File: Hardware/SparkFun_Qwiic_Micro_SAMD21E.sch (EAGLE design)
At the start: 41 parts, among them Q1 3.1A/30V/105mΩ, U1 3.3V, U2 W25Q32FV, U3 SAMD21E

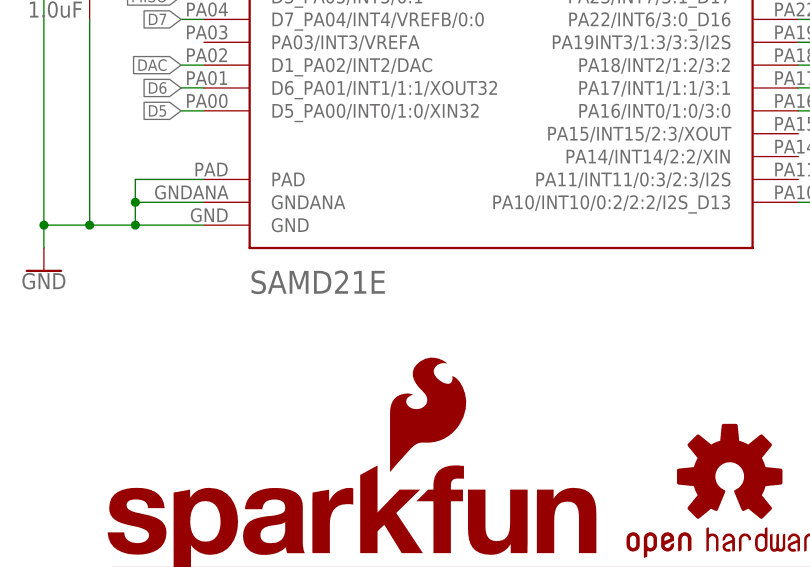
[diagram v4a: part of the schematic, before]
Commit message: New bootloader, updates samd21 with latest package
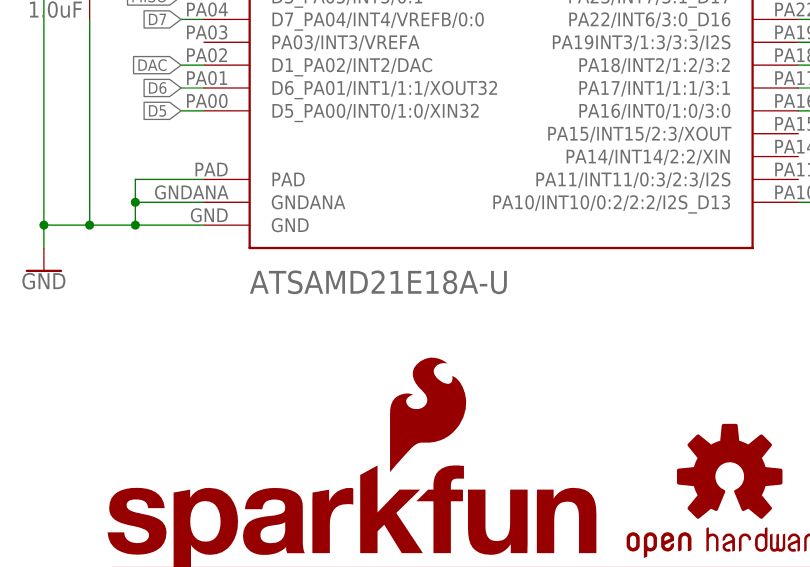
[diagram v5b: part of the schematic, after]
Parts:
- U3: value SAMD21E -> ATSAMD21E18A-U; device SparkFun-IC-Microcontroller:SAMD21E -> SparkFun-IC-Microcontroller:ATSAMD21E18A-U
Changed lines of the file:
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@@
 <part name="GND3" library="SparkFun-PowerSymbols" deviceset="GND" device=""/>
 <part name="SUPPLY14" library="SparkFun-PowerSymbols" deviceset="V_USB" device=""/>
-<part name="U3" library="SparkFun-IC-Microcontroller" deviceset="SAMD21E" device=""/>
+<part name="U3" library="SparkFun-IC-Microcontroller" deviceset="ATSAMD21E18A-U" device=""/>
 <part name="SUPPLY11" library="SparkFun-PowerSymbols" deviceset="V_USB" device=""/>
 <part name="JP1" library="SparkFun-Jumpers" deviceset="JUMPER-SMT_2_NC_TRACE" device="_SILK" value="LED"/>

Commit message: Moves 10k pull-up resistor on Flash CS line to top layer.
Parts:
- R2: device SparkFun-Resistors:10KOHM-0603-1/10W-1% -> SparkFun-Resistors:10KOHM-0402-1/16W-1%
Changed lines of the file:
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@@
 <?xml version="1.0" encoding="utf-8"?>
 <!DOCTYPE eagle SYSTEM "eagle.dtd">
-<eagle version="9.4.0">
+<eagle version="9.4.2">
 <drawing>
 <settings>
@@
 <part name="GND8" library="SparkFun-PowerSymbols" deviceset="GND" device=""/>
 <part name="GND4" library="SparkFun-PowerSymbols" deviceset="GND" device=""/>
-<part name="R2" library="SparkFun-Resistors" deviceset="10KOHM" device="-0603-1/10W-1%" value="10k"/>
+<part name="R2" library="SparkFun-Resistors" deviceset="10KOHM" device="-0402-1/16W-1%" value="10k"/>
 <part name="SUPPLY8" library="SparkFun-PowerSymbols" deviceset="3.3V" device=""/>
 <part name="D1" library="SparkFun-DiscreteSemi" deviceset="DIODE-SCHOTTKY" device="-BAT20J" value="1A/23V/620mV"/>

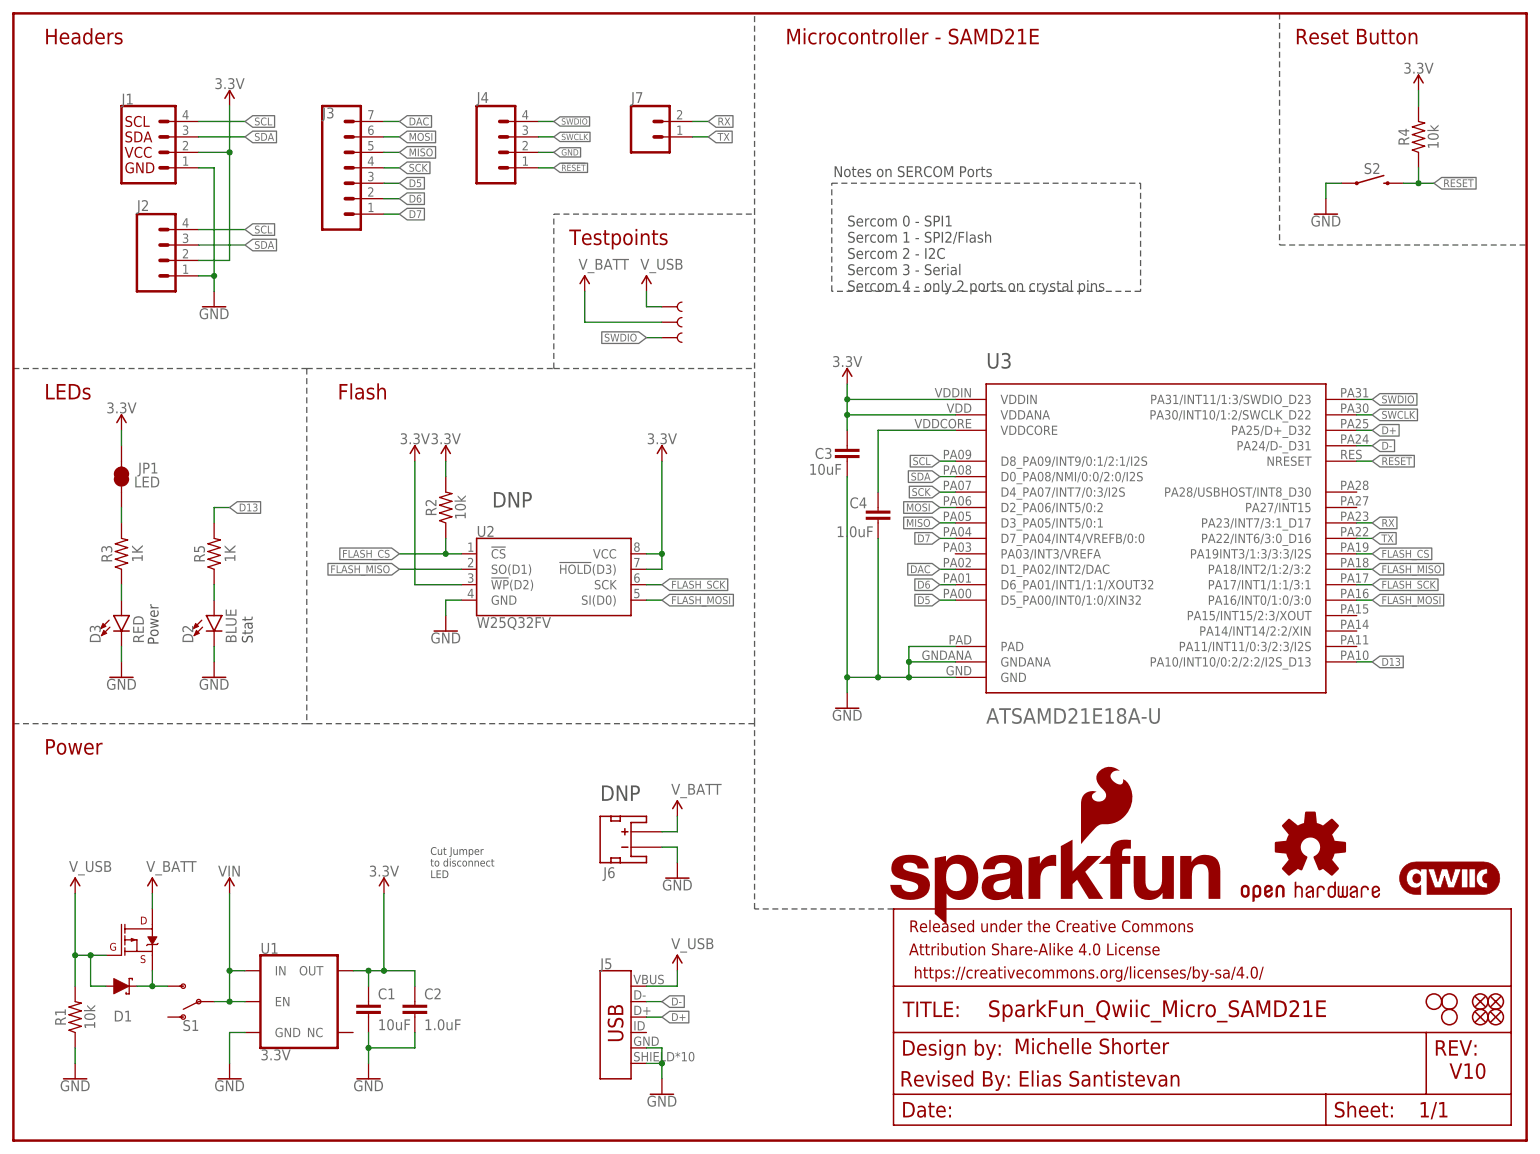
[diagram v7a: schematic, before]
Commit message: Adds VCC ranges, Adds note for optional parts
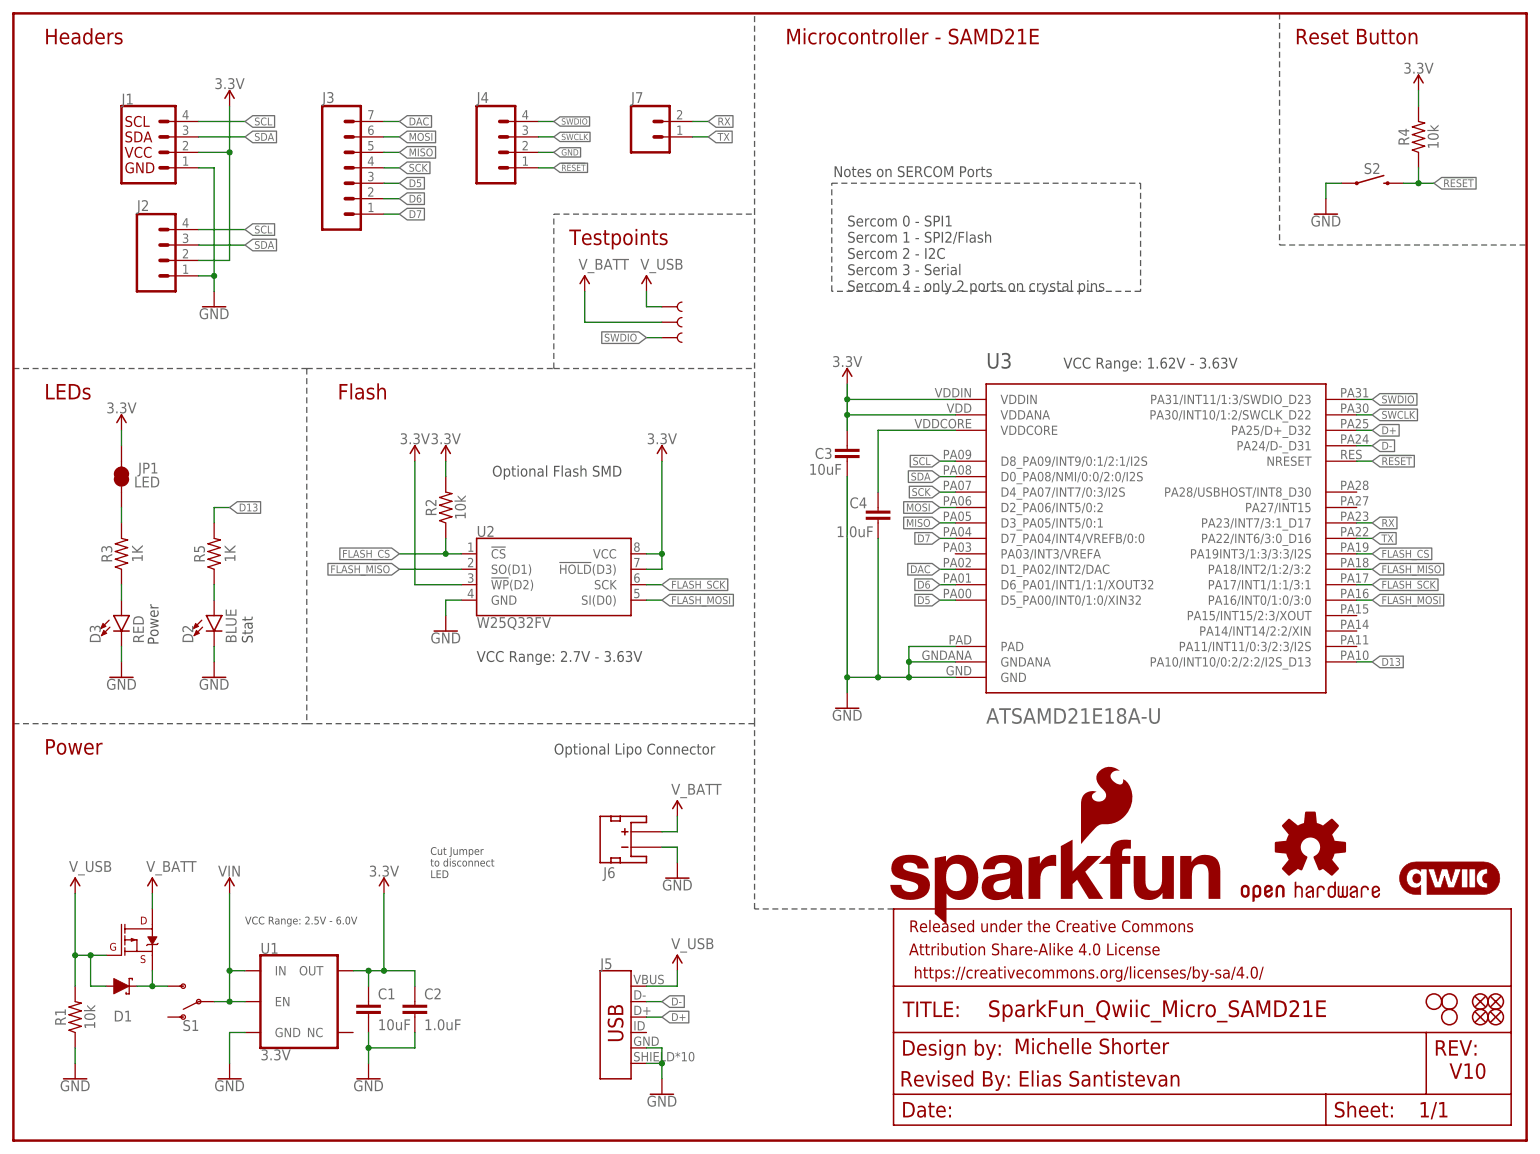
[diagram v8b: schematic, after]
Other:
- note added: "Optional Flash SMD"
- note added: "Optional Lipo Connector"
- note added: "VCC Range: 1.62V - 3.63V"
- note added: "VCC Range: 2.5V - 6.0V"
- note added: "VCC Range: 2.7V - 3.63V"
- note removed: "DNP"
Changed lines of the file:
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@@
 <?xml version="1.0" encoding="utf-8"?>
 <!DOCTYPE eagle SYSTEM "eagle.dtd">
-<eagle version="9.4.0">
+<eagle version="9.4.2">
 <drawing>
 <settings>
@@
 <text x="5.08" y="63.5" size="2.54" layer="94" font="vector">Power</text>
 <text x="127" y="180.34" size="2.54" layer="94" font="vector">Microcontroller - SAMD21E</text>
-<text x="78.74" y="104.14" size="2.54" layer="97" font="vector">DNP</text>
-<text x="96.52" y="55.88" size="2.54" layer="97" font="vector">DNP</text>
+<text x="78.74" y="109.22" size="1.778" layer="97" font="vector">Optional Flash SMD</text>
 <text x="236.22" y="10.16" size="2.54" layer="94" font="vector">V10</text>
 <text x="164.592" y="14.224" size="2.54" layer="94" font="vector">Michelle Shorter</text>
@@
 <text x="39.37" y="81.788" size="1.778" layer="97" font="vector" rot="R90">Stat</text>
 <text x="23.876" y="81.534" size="1.778" layer="97" font="vector" rot="R90">Power</text>
+<text x="38.1" y="35.56" size="1.27" layer="97" font="vector">VCC Range: 2.5V - 6.0V</text>
+<text x="172.72" y="127" size="1.778" layer="97" font="vector">VCC Range: 1.62V - 3.63V</text>
+<text x="76.2" y="78.74" size="1.778" layer="97" font="vector">VCC Range: 2.7V - 3.63V</text>
+<text x="88.9" y="63.5" size="1.778" layer="97" font="vector">Optional Lipo Connector</text>
 </plain>
 <instances>
@@
 <instance part="J3" gate="J1" x="55.88" y="157.48" smashed="yes">
 <attribute name="VALUE" x="50.8" y="147.574" size="1.778" layer="96" font="vector"/>
-<attribute name="NAME" x="50.8" y="168.148" size="1.778" layer="95" font="vector"/>
+<attribute name="NAME" x="50.8" y="170.688" size="1.778" layer="95" font="vector"/>
 </instance>
 <instance part="J7" gate="G$1" x="104.14" y="165.1" smashed="yes">
